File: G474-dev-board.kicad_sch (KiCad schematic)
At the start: 39 parts, among them J1 Conn_01x03, J16 Conn_01x02, J2 Conn_01x02, J8 ST-LINK, SW1 SW_Push, SW2 SW_Push, U1 STM32G474RETx, Y1 24MHz, Y3 32.768KHz

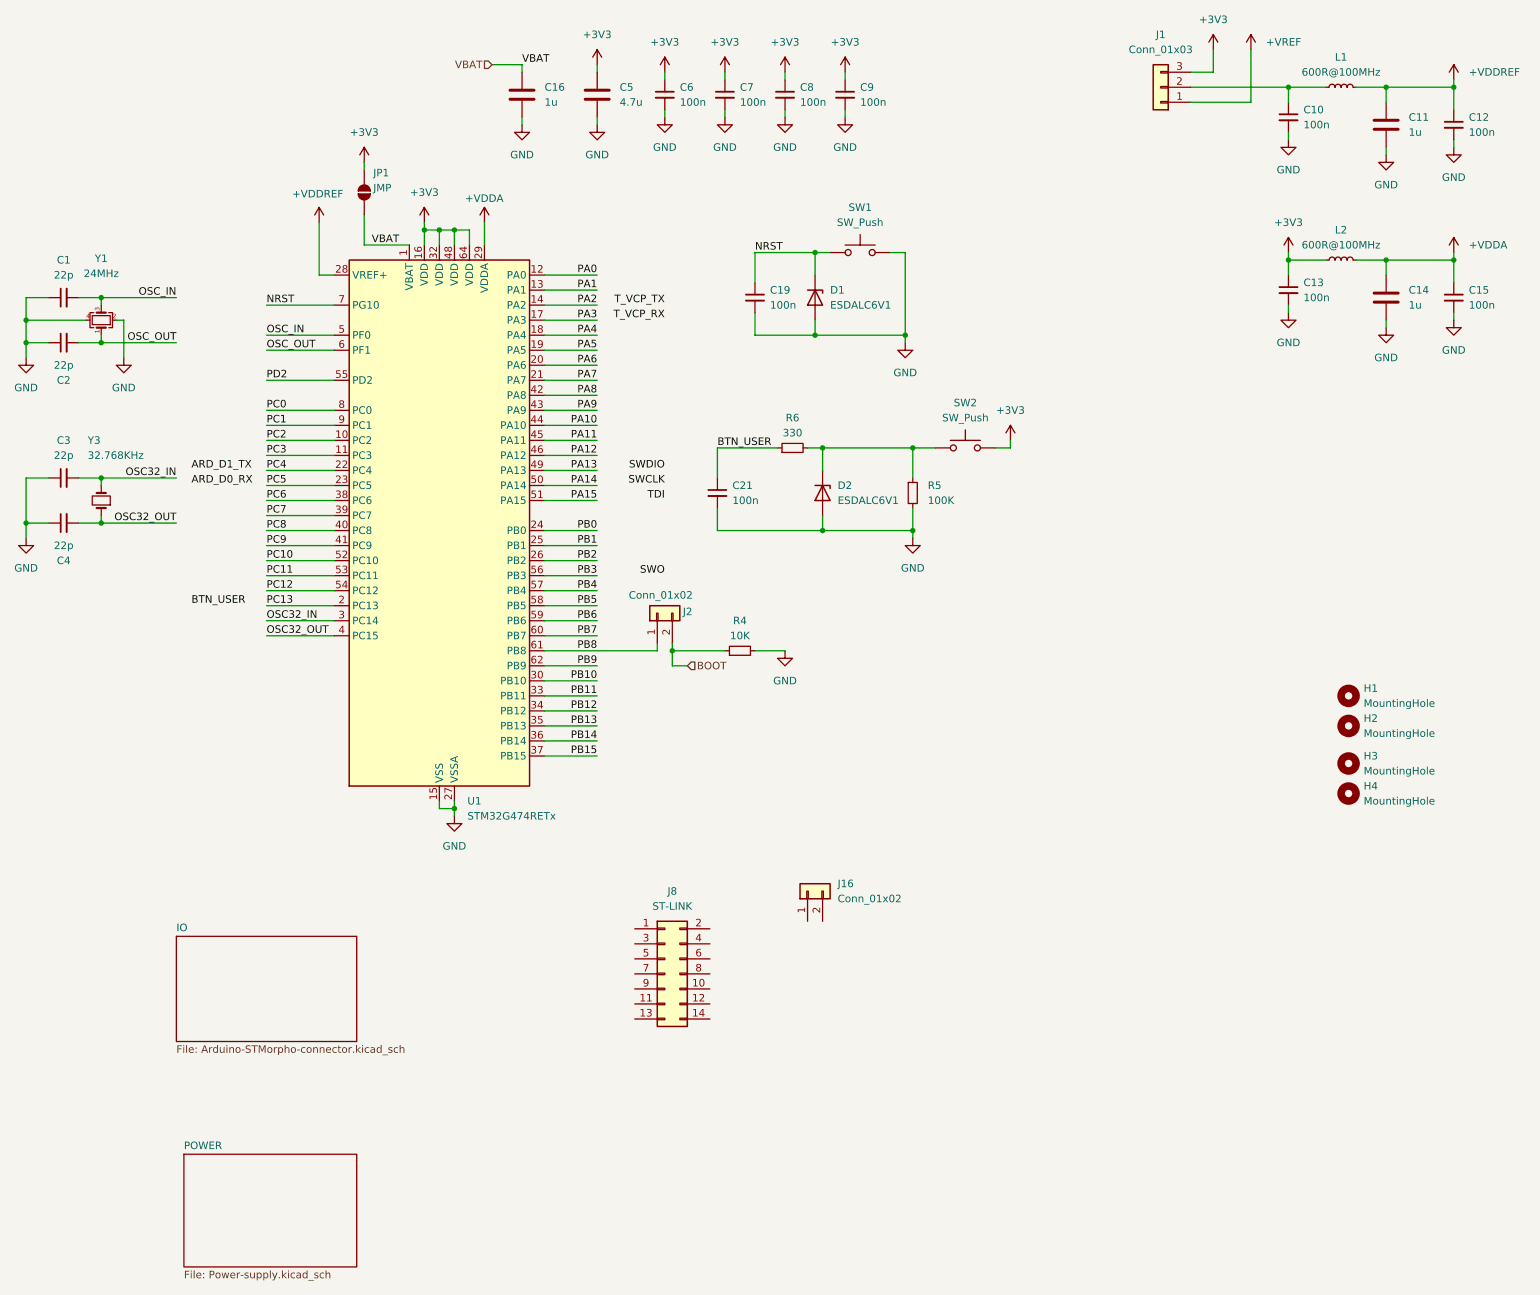
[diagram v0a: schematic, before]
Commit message: SMD part number assigned, relocate MCU sch to hierarcical sheet
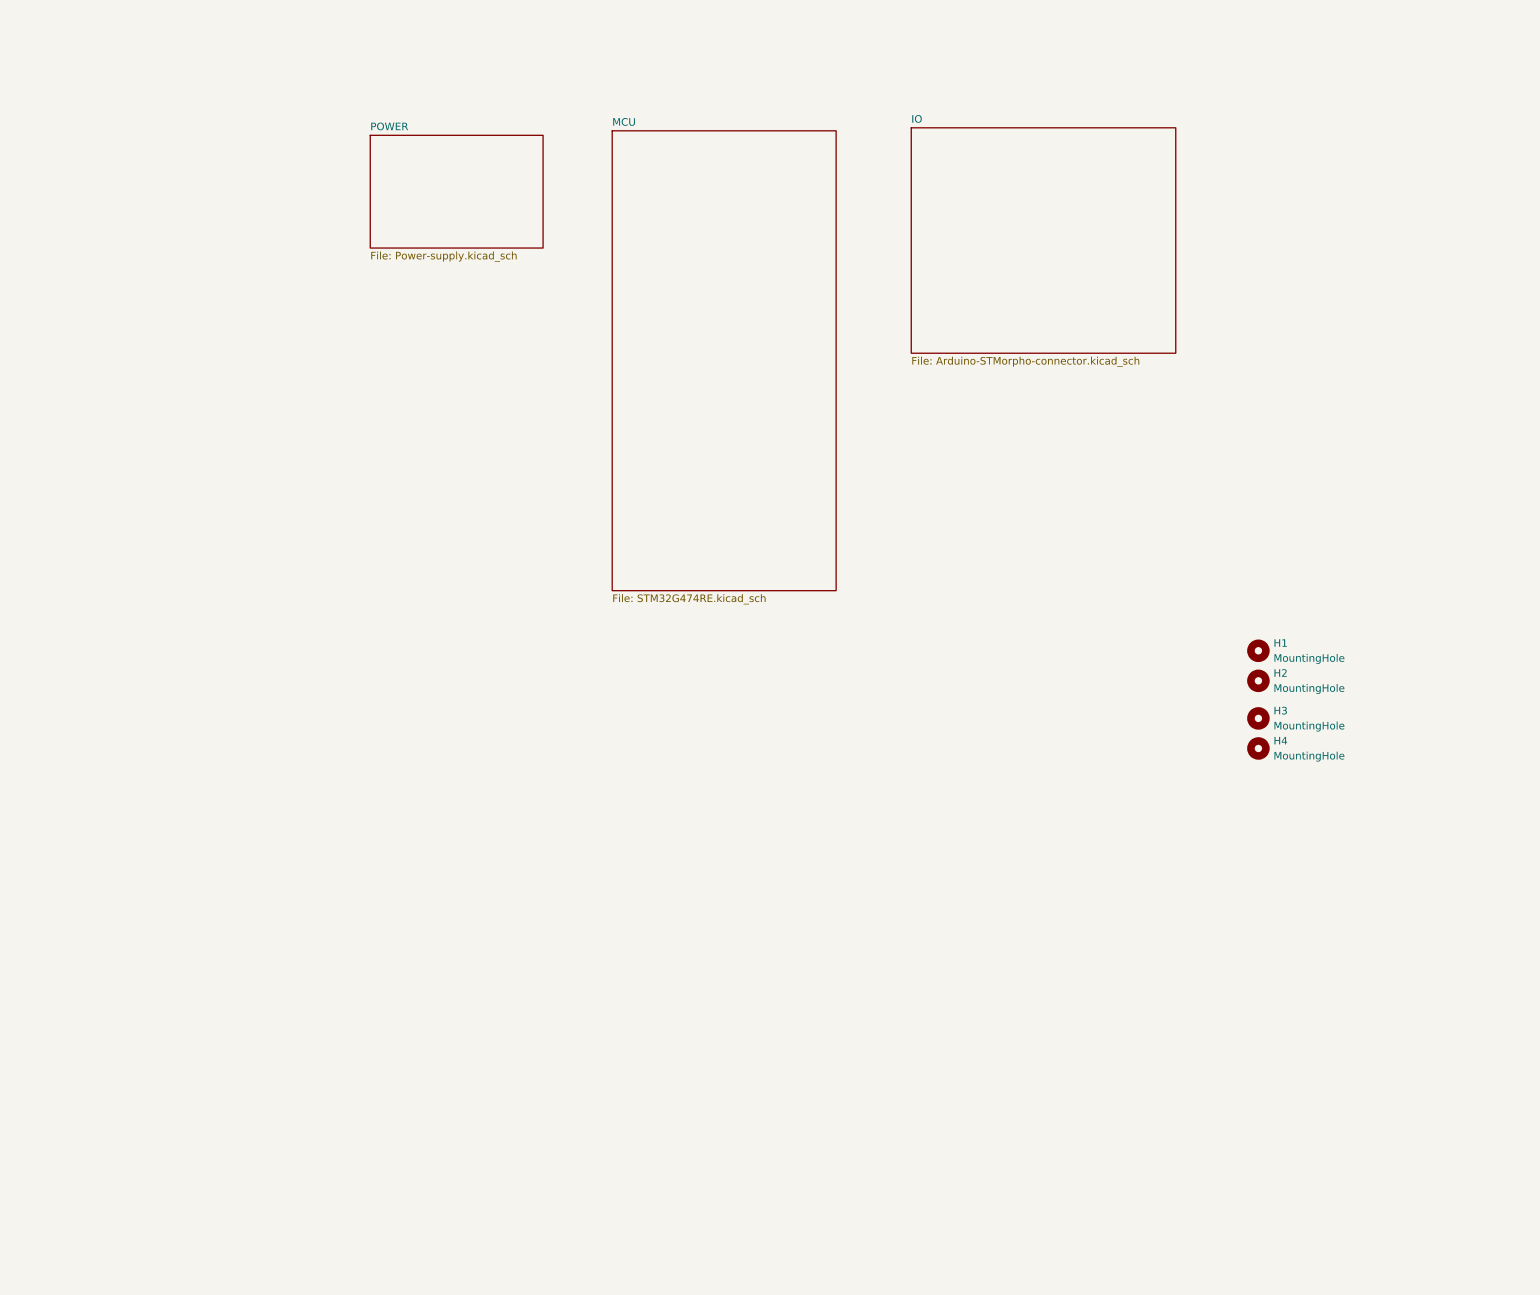
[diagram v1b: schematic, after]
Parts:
- removed C1, C2, C3, C4: 22p, Capacitor_SMD:C_0603_1608Metric, symbol Device:C_Small
- removed C10, C12, C13, C15, C19, C21, C6, C7, C8, C9: 100n, Capacitor_SMD:C_0603_1608Metric, symbol Device:C_Small
- removed C11, C14, C16: 1u, Capacitor_SMD:C_0805_2012Metric, symbol Device:C
- removed C5: 4.7u, Capacitor_SMD:C_0805_2012Metric, symbol Device:C
- removed D1, D2: ESDALC6V1, Diode_SMD:D_SOD-523, symbol Diode:ESD5Zxx
- removed J1: Conn_01x03, Connector_PinHeader_2.54mm:PinHeader_1x03_P2.54mm_Vertical, symbol Connector_Generic:Conn_01x03
- removed J16, J2: Conn_01x02, Connector_PinHeader_2.54mm:PinHeader_1x02_P2.54mm_Vertical, symbol Connector_Generic:Conn_01x02
- removed J8: ST-LINK, Connector_PinHeader_1.27mm:PinHeader_2x07_P1.27mm_Vertical_SMD, symbol Connector_Generic:Conn_02x07_Odd_Even
- removed JP1: JMP, Jumper:SolderJumper-2_P1.3mm_Open_RoundedPad1.0x1.5mm, symbol Jumper:SolderJumper_2_Open
- removed L1, L2: 600R@100MHz, Inductor_SMD:L_0805_2012Metric_Pad1.05x1.20mm_HandSolder, symbol Device:L_Small
- removed R4: 10K, Resistor_SMD:R_0603_1608Metric, symbol Device:R_Small
- removed R5: 100K, Resistor_SMD:R_0603_1608Metric, symbol Device:R_Small
- removed R6: 330, Resistor_SMD:R_0603_1608Metric, symbol Device:R_Small
- removed SW1, SW2: SW_Push, Button_Switch_THT:SW_PUSH_6mm_H5mm, symbol Switch:SW_Push
- removed U1: STM32G474RETx, Package_QFP:LQFP-64_10x10mm_P0.5mm, symbol MCU_ST_STM32G4:STM32G474RETx
- removed Y1: 24MHz, Crystal:Crystal_SMD_3225-4Pin_3.2x2.5mm, symbol Device:Crystal_GND24_Small
- removed Y3: 32.768KHz, Crystal:Crystal_SMD_3215-2Pin_3.2x1.5mm, symbol Device:Crystal_Small
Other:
- added sheet MCU (STM32G474RE.kicad_sch)
- moved on the sheet: H1, H2, H3, H4

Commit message: no changes
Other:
- sheet IO ports: added BOOT, NRST, PA[0..15], PB[0..15], PC[0..15], PD2, VBAT; removed none
- sheet MCU ports: added BOOT, NRST, PA[0..15], PB[0..15], PC[0..15], PD2, VBAT; removed none
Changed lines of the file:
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@@
 	(generator_version "8.0")
 	(paper "A4")
+	(wire
+		(pts
+			(xy 160.02 50.8) (xy 172.72 50.8)
+		)
+		(stroke
+			(width 0)
+			(type default)
+		)
+	)
+	(bus
+		(pts
+			(xy 160.02 45.72) (xy 172.72 45.72)
+		)
+		(stroke
+			(width 0)
+			(type default)
+		)
+	)
+	(bus
+		(pts
+			(xy 160.02 48.26) (xy 172.72 48.26)
+		)
+		(stroke
+			(width 0)
+			(type default)
+		)
+	)
+	(wire
+		(pts
+			(xy 160.02 54.61) (xy 172.72 54.61)
+		)
+		(stroke
+			(width 0)
+			(type default)
+		)
+	)
+	(wire
+		(pts
+			(xy 160.02 39.37) (xy 172.72 39.37)
+		)
+		(stroke
+			(width 0)
+			(type default)
+		)
+	)
+	(wire
+		(pts
+			(xy 160.02 57.15) (xy 172.72 57.15)
+		)
+		(stroke
+			(width 0)
+			(type default)
+		)
+	)
+	(bus
+		(pts
+			(xy 160.02 43.18) (xy 172.72 43.18)
+		)
+		(stroke
+			(width 0)
+			(type default)
+		)
+	)
 	(symbol
 		(lib_id "Mechanical:MountingHole")
@@
 	)
 	(sheet
-		(at 121.92 36.576)
-		(size 37.846 77.724)
+		(at 121.92 35.56)
+		(size 38.1 78.74)
 		(fields_autoplaced yes)
 		(stroke
@@
 		)
 		(property "Sheetname" "MCU"
-			(at 121.92 35.8644 0)
+			(at 121.92 34.8484 0)
 			(effects
 				(font
@@
 				)
 				(justify left top)
+			)
+		)
+		(pin "VBAT" input
+			(at 160.02 39.37 0)
+			(effects
+				(font
+					(size 1.27 1.27)
+				)
+				(justify right)
+			)
+		)
+		(pin "PB[0..15]" bidirectional
+			(at 160.02 45.72 0)
+			(effects
+				(font
+					(size 1.27 1.27)
+				)
+				(justify right)
+			)
+		)
+		(pin "BOOT" input
+			(at 160.02 57.15 0)
+			(effects
+				(font
+					(size 1.27 1.27)
+				)
+				(justify right)
+			)
+		)
+		(pin "PC[0..15]" bidirectional
+			(at 160.02 48.26 0)
+			(effects
+				(font
+					(size 1.27 1.27)
+				)
+				(justify right)
+			)
+		)
+		(pin "NRST" input
+			(at 160.02 54.61 0)
+			(effects
+				(font
+					(size 1.27 1.27)
+				)
+				(justify right)
+			)
+		)
+		(pin "PA[0..15]" bidirectional
+			(at 160.02 43.18 0)
+			(effects
+				(font
+					(size 1.27 1.27)
+				)
+				(justify right)
+			)
+		)
+		(pin "PD2" bidirectional
+			(at 160.02 50.8 0)
+			(effects
+				(font
+					(size 1.27 1.27)
+				)
+				(justify right)
 			)
 		)
@@
 	)
 	(sheet
-		(at 172.466 36.068)
-		(size 44.704 38.1)
+		(at 172.72 35.56)
+		(size 44.45 24.13)
 		(fields_autoplaced yes)
 		(stroke
@@
 		)
 		(property "Sheetname" "IO"
-			(at 172.466 35.3564 0)
+			(at 172.72 34.8484 0)
 			(effects
 				(font
@@
 		)
 		(property "Sheetfile" "Arduino-STMorpho-connector.kicad_sch"
-			(at 172.466 74.7526 0)
+			(at 172.72 60.2746 0)
 			(effects
 				(font
@@
 			)
 		)
+		(pin "VBAT" output
+			(at 172.72 39.37 180)
+			(effects
+				(font
+					(size 1.27 1.27)
+				)
+				(justify left)
+			)
+		)
+		(pin "PC[0..15]" bidirectional
+			(at 172.72 48.26 180)
+			(effects
+				(font
+					(size 1.27 1.27)
+				)
+				(justify left)
+			)
+		)
+		(pin "NRST" output
+			(at 172.72 54.61 180)
+			(effects
+				(font
+					(size 1.27 1.27)
+				)
+				(justify left)
+			)
+		)
+		(pin "BOOT" output
+			(at 172.72 57.15 180)
+			(effects
+				(font
+					(size 1.27 1.27)
+				)
+				(justify left)
+			)
+		)
+		(pin "PB[0..15]" bidirectional
+			(at 172.72 45.72 180)
+			(effects
+				(font
+					(size 1.27 1.27)
+				)
+				(justify left)
+			)
+		)
+		(pin "PA[0..15]" bidirectional
+			(at 172.72 43.18 180)
+			(effects
+				(font
+					(size 1.27 1.27)
+				)
+				(justify left)
+			)
+		)
+		(pin "PD2" bidirectional
+			(at 172.72 50.8 180)
+			(effects
+				(font
+					(size 1.27 1.27)
+				)
+				(justify left)
+			)
+		)
